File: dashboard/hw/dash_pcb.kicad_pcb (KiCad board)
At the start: 2 copper layers, 180 x 65 mm, 33 parts, among them J1 LCD, J2 DEBUG, J3 LCD_BL, J4 CAR, U1 LPC11C24FBD48, U3 TLV70233_SOT23-5, Y1 12MHz

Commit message: add footprint for TI power chip
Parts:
- added U2: TPS62175, custom_footprints:DQC, F.Cu at (164.5, 78.5)
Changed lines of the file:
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@@
 (kicad_pcb (version 4) (host pcbnew 4.0.7)
   (general
-    (links 88)
-    (no_connects 79)
+    (links 101)
+    (no_connects 89)
     (area 84.924999 54.924999 265.075001 120.075001)
     (thickness 1.6)
@@
     (tracks 83)
     (zones 0)
-    (modules 33)
-    (nets 60)
+    (modules 34)
+    (nets 61)
   )
   (page A4)
@@
   (net 58 +BATT)
   (net 59 "Net-(U1-Pad45)")
+  (net 60 "Net-(L1-Pad1)")
   (net_class Default "This is the default net class."
     (clearance 0.15)
@@
     (add_net "Net-(J2-Pad8)")
     (add_net "Net-(J3-Pad2)")
+    (add_net "Net-(L1-Pad1)")
     (add_net "Net-(R1-Pad1)")
     (add_net "Net-(R10-Pad1)")
@@
     )
   )
+  (module custom_footprints:DQC (layer F.Cu)
+    (at 164.5 78.45)
+    (solder_mask_margin 0.07)
+    (solder_paste_ratio -0.17)
+    (fp_text reference U2 (at 0 2.5) (layer F.SilkS)
+      (effects (font (size 1 1) (thickness 0.15)))
+    )
+    (fp_text value TPS62175 (at 0 -2.5) (layer F.Fab)
+      (effects (font (size 1 1) (thickness 0.15)))
+    )
+    (fp_line (start -1.5 -1.5) (end -1 -1.5) (layer F.SilkS) (width 0.15))
+    (fp_line (start -1.5 -1) (end -1.5 -1.5) (layer F.SilkS) (width 0.15))
+    (fp_line (start -1 1.5) (end 1 1.5) (layer F.CrtYd) (width 0.15))
+    (fp_line (start -1 -1.5) (end 1 -1.5) (layer F.CrtYd) (width 0.15))
+    (pad 1 smd rect (at -0.95 -1) (size 0.5 0.25) (layers F.Cu F.Paste F.Mask)
+      (net 1 GND) (solder_mask_margin 0.07))
+    (pad 2 smd rect (at -0.95 -0.5 180) (size 0.5 0.25) (layers F.Cu F.Paste F.Mask)
+      (net 58 +BATT) (solder_mask_margin 0.07))
+    (pad 3 smd rect (at -0.95 0) (size 0.5 0.25) (layers F.Cu F.Paste F.Mask)
+      (net 58 +BATT) (solder_mask_margin 0.07))
+    (pad 4 smd rect (at -0.95 0.5) (size 0.5 0.25) (layers F.Cu F.Paste F.Mask)
+      (net 1 GND) (solder_mask_margin 0.07))
+    (pad 5 smd rect (at -0.95 1) (size 0.5 0.25) (layers F.Cu F.Paste F.Mask)
+      (net 56 "Net-(R10-Pad1)") (solder_mask_margin 0.07))
+    (pad 6 smd rect (at 0.95 1) (size 0.5 0.25) (layers F.Cu F.Paste F.Mask)
+      (net 1 GND) (solder_mask_margin 0.07))
+    (pad 7 smd rect (at 0.95 0.5) (size 0.5 0.25) (layers F.Cu F.Paste F.Mask)
+      (net 55 /5VPG) (solder_mask_margin 0.07))
+    (pad 8 smd rect (at 0.95 0) (size 0.5 0.25) (layers F.Cu F.Paste F.Mask)
+      (net 2 +5V) (solder_mask_margin 0.07))
+    (pad 9 smd rect (at 0.95 -0.5) (size 0.5 0.25) (layers F.Cu F.Paste F.Mask)
+      (net 60 "Net-(L1-Pad1)") (solder_mask_margin 0.07))
+    (pad 10 smd rect (at 0.95 -1) (size 0.5 0.25) (layers F.Cu F.Paste F.Mask)
+      (net 2 +5V) (solder_mask_margin 0.07))
+    (pad 1 smd rect (at 0 0) (size 0.84 2.4) (layers F.Cu F.Paste F.Mask)
+      (net 1 GND) (solder_paste_margin -0.04) (solder_paste_margin_ratio -0.00001))
+    (pad 1 thru_hole circle (at 0 0) (size 0.4 0.4) (drill 0.2) (layers *.Cu *.Mask)
+      (net 1 GND) (solder_mask_margin 0.04) (solder_paste_margin -0.001) (solder_paste_margin_ratio -0.00001))
+    (pad 1 thru_hole circle (at 0 0.95) (size 0.4 0.4) (drill 0.2) (layers *.Cu *.Mask)
+      (net 1 GND) (solder_mask_margin 0.04) (solder_paste_margin -0.001) (solder_paste_margin_ratio -0.00001))
+    (pad 1 thru_hole circle (at 0 -0.95) (size 0.4 0.4) (drill 0.2) (layers *.Cu *.Mask)
+      (net 1 GND) (solder_mask_margin 0.04) (solder_paste_margin -0.001) (solder_paste_margin_ratio -0.00001))
+  )
   (gr_line (start 265 120) (end 265 55) (layer Edge.Cuts) (width 0.15))

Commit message: add footprint for contrast pot
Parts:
- RV1: footprint Potentiometers:Potentiometer_Trimmer_ACP_CA6h_Vertical -> custom_footprints:Bourns_3362X
- moved RV1 17.3 mm to (252.5, 57.4)
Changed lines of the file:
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@@
-    )
-  )
-  (module Potentiometers:Potentiometer_Trimmer_ACP_CA6h_Vertical (layer F.Cu)
-    (at 244 72.5)
-    (descr "Potentiometer, vertically mounted, Omeg PC16PU, Omeg PC16PU, Omeg PC16PU, Vishay/Spectrol 248GJ/249GJ Single, Vishay/Spectrol 248GJ/249GJ Single, Vishay/Spectrol 248GJ/249GJ Single, Vishay/Spectrol 248GH/249GH Single, Vishay/Spectrol 148/149 Single, Vishay/Spectrol 148/149 Single, Vishay/Spectrol 148/149 Single, Vishay/Spectrol 148A/149A Single with mounting plates, Vishay/Spectrol 148/149 Double, Vishay/Spectrol 148A/149A Double with mounting plates, Piher PC-16 Single, Piher PC-16 Single, Piher PC-16 Single, Piher PC-16SV Single, Piher PC-16 Double, Piher PC-16 Triple, Piher T16H Single, Piher T16L Single, Piher T16H Double, Alps RK163 Single, Alps RK163 Double, Alps RK097 Single, Alps RK097 Double, Bourns PTV09A-2 Single with mounting sleve Single, Bourns PTV09A-1 with mounting sleve Single, Bourns PRS11S Single, Alps RK09K Single with mounting sleve Single, Alps RK09K with mounting sleve Single, Alps RK09L Single, Alps RK09L Single, Alps RK09L Double, Alps RK09L Double, Alps RK09Y Single, Bourns 3339S Single, Bourns 3339S Single, Bourns 3339P Single, Bourns 3339H Single, Vishay T7YA Single, Suntan TSR-3386H Single, Suntan TSR-3386H Single, Suntan TSR-3386P Single, Vishay T73XX Single, Vishay T73XX Single, Vishay T73YP Single, Piher PT-6h Single, Piher PT-6v Single, Piher PT-6v Single, Piher PT-10h2.5 Single, Piher PT-10h5 Single, Piher PT-101h3.8 Single, Piher PT-10v10 Single, Piher PT-10v10 Single, Piher PT-10v5 Single, Piher PT-15h5 Single, Piher PT-15h2.5 Single, Piher PT-15B Single, Piher PT-15hc5 Single, Piher PT-15v12.5 Single, Piher PT-15v12.5 Single, Piher PT-15v15 Single, Piher PT-15v15 Single, ACP CA6h Single, http://www.acptechnologies.com/wp-content/uploads/2016/12/ACP-CAT%C3%81LOGO-ENTERO-2016.pdf")
-    (tags "Potentiometer vertical  Omeg PC16PU  Omeg PC16PU  Omeg PC16PU  Vishay/Spectrol 248GJ/249GJ Single  Vishay/Spectrol 248GJ/249GJ Single  Vishay/Spectrol 248GJ/249GJ Single  Vishay/Spectrol 248GH/249GH Single  Vishay/Spectrol 148/149 Single  Vishay/Spectrol 148/149 Single  Vishay/Spectrol 148/149 Single  Vishay/Spectrol 148A/149A Single with mounting plates  Vishay/Spectrol 148/149 Double  Vishay/Spectrol 148A/149A Double with mounting plates  Piher PC-16 Single  Piher PC-16 Single  Piher PC-16 Single  Piher PC-16SV Single  Piher PC-16 Double  Piher PC-16 Triple  Piher T16H Single  Piher T16L Single  Piher T16H Double  Alps RK163 Single  Alps RK163 Double  Alps RK097 Single  Alps RK097 Double  Bourns PTV09A-2 Single with mounting sleve Single  Bourns PTV09A-1 with mounting sleve Single  Bourns PRS11S Single  Alps RK09K Single with mounting sleve Single  Alps RK09K with mounting sleve Single  Alps RK09L Single  Alps RK09L Single  Alps RK09L Double  Alps RK09L Double  Alps RK09Y Single  Bourns 3339S Single  Bourns 3339S Single  Bourns 3339P Single  Bourns 3339H Single  Vishay T7YA Single  Suntan TSR-3386H Single  Suntan TSR-3386H Single  Suntan TSR-3386P Single  Vishay T73XX Single  Vishay T73XX Single  Vishay T73YP Single  Piher PT-6h Single  Piher PT-6v Single  Piher PT-6v Single  Piher PT-10h2.5 Single  Piher PT-10h5 Single  Piher PT-101h3.8 Single  Piher PT-10v10 Single  Piher PT-10v10 Single  Piher PT-10v5 Single  Piher PT-15h5 Single  Piher PT-15h2.5 Single  Piher PT-15B Single  Piher PT-15hc5 Single  Piher PT-15v12.5 Single  Piher PT-15v12.5 Single  Piher PT-15v15 Single  Piher PT-15v15 Single  ACP CA6h Single")
-    (fp_text reference RV1 (at 0 -2.06) (layer F.SilkS)
-      (effects (font (size 1 1) (thickness 0.15)))
-    )
-    (fp_text value 10k (at 0 7.06) (layer F.Fab)
-      (effects (font (size 1 1) (thickness 0.15)))
-    )
-    (fp_line (start 3.5 -0.65) (end 3.5 5.65) (layer F.Fab) (width 0.1))
-    (fp_line (start 3.5 5.65) (end 0 5.65) (layer F.Fab) (width 0.1))
-    (fp_line (start 0 5.65) (end 0 -0.65) (layer F.Fab) (width 0.1))
-    (fp_line (start 0 -0.65) (end 3.5 -0.65) (layer F.Fab) (width 0.1))
-    (fp_line (start 0 1.5) (end 0 3.5) (layer F.Fab) (width 0.1))
-    (fp_line (start 0 3.5) (end 3.5 3.5) (layer F.Fab) (width 0.1))
-    (fp_line (start 3.5 3.5) (end 3.5 1.5) (layer F.Fab) (width 0.1))
-    (fp_line (start 3.5 1.5) (end 0 1.5) (layer F.Fab) (width 0.1))
-    (fp_line (start 0.873 -0.71) (end 3.56 -0.71) (layer F.SilkS) (width 0.12))
-    (fp_line (start 0.873 5.71) (end 3.56 5.71) (layer F.SilkS) (width 0.12))
-    (fp_line (start 3.56 -0.71) (end 3.56 5.71) (layer F.SilkS) (width 0.12))
-    (fp_line (start -0.061 1.005) (end -0.061 3.996) (layer F.SilkS) (width 0.12))
-    (fp_line (start -0.061 1.44) (end 3.56 1.44) (layer F.SilkS) (width 0.12))
-    (fp_line (start -0.061 3.56) (end 3.56 3.56) (layer F.SilkS) (width 0.12))
-    (fp_line (start -0.061 1.44) (end -0.061 3.56) (layer F.SilkS) (width 0.12))
-    (fp_line (start 3.56 1.44) (end 3.56 3.56) (layer F.SilkS) (width 0.12))
-    (fp_line (start -1.1 -1.1) (end -1.1 6.1) (layer F.CrtYd) (width 0.05))
-    (fp_line (start -1.1 6.1) (end 3.75 6.1) (layer F.CrtYd) (width 0.05))
-    (fp_line (start 3.75 6.1) (end 3.75 -1.1) (layer F.CrtYd) (width 0.05))
-    (fp_line (start 3.75 -1.1) (end -1.1 -1.1) (layer F.CrtYd) (width 0.05))
-    (pad 3 thru_hole circle (at 0 5) (size 1.62 1.62) (drill 0.9) (layers *.Cu *.Mask)
-      (net 1 GND))
-    (pad 2 thru_hole circle (at 2.5 2.5) (size 1.62 1.62) (drill 0.9) (layers *.Cu *.Mask)
-      (net 3 /LCD_V0))
-    (pad 1 thru_hole circle (at 0 0) (size 1.62 1.62) (drill 0.9) (layers *.Cu *.Mask)
-      (net 15 /LCD_VEE))
-    (model Potentiometers.3dshapes/Potentiometer_Trimmer_ACP_CA6h_Vertical.wrl
-      (at (xyz 0 0 0))
-      (scale (xyz 0.393701 0.393701 0.393701))
-      (rotate (xyz 0 0 0))
     )
   )
@@
       (net 1 GND) (solder_mask_margin 0.04) (solder_paste_margin -0.001) (solder_paste_margin_ratio -0.00001))
   )
+  (module custom_footprints:Bourns_3362X (layer F.Cu)
+    (at 252.476 57.404)
+    (fp_text reference RV1 (at -1.27 3.302) (layer F.SilkS)
+      (effects (font (size 1 1) (thickness 0.15)))
+    )
+    (fp_text value 10k (at 0 -3.048) (layer F.Fab)
+      (effects (font (size 1 1) (thickness 0.15)))
+    )
+    (fp_line (start -3.302 -2.286) (end -3.302 1.016) (layer F.SilkS) (width 0.15))
+    (fp_line (start 3.302 -2.286) (end -3.302 -2.286) (layer F.SilkS) (width 0.15))
+    (fp_line (start 3.302 2.286) (end 3.302 -2.286) (layer F.SilkS) (width 0.15))
+    (fp_line (start 1.778 2.286) (end 3.302 2.286) (layer F.SilkS) (width 0.15))
+    (fp_line (start 1.778 1.778) (end 1.778 2.286) (layer F.SilkS) (width 0.15))
+    (fp_line (start -1.778 1.778) (end 1.778 1.778) (layer F.SilkS) (width 0.15))
+    (fp_line (start -1.778 2.286) (end -1.778 1.778) (layer F.SilkS) (width 0.15))
+    (fp_line (start -3.302 2.286) (end -1.778 2.286) (layer F.SilkS) (width 0.15))
+    (fp_line (start -3.302 1.016) (end -3.302 2.286) (layer F.SilkS) (width 0.15))
+    (fp_line (start 3.302 2.286) (end 0 2.286) (layer F.CrtYd) (width 0.15))
+    (fp_line (start 3.302 -2.286) (end 3.302 2.286) (layer F.CrtYd) (width 0.15))
+    (fp_line (start -3.302 -2.286) (end 3.302 -2.286) (layer F.CrtYd) (width 0.15))
+    (fp_line (start -3.302 2.286) (end -3.302 -2.286) (layer F.CrtYd) (width 0.15))
+    (fp_line (start 0 2.286) (end -3.302 2.286) (layer F.CrtYd) (width 0.15))
+    (pad 2 thru_hole circle (at 0 -1.27) (size 1 1) (drill 0.5) (layers *.Cu *.Mask)
+      (net 3 /LCD_V0))
+    (pad 3 thru_hole circle (at -2.54 1.27) (size 1 1) (drill 0.5) (layers *.Cu *.Mask)
+      (net 1 GND))
+    (pad 1 thru_hole circle (at 2.54 1.27) (size 1 1) (drill 0.5) (layers *.Cu *.Mask)
+      (net 15 /LCD_VEE))
+  )
   (gr_line (start 265 120) (end 265 55) (layer Edge.Cuts) (width 0.15))

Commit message: add footprint for inductor
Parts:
- added L1: 10u, custom_footprints:Coilcraft_LPS4018, F.Cu at (170.7, 71.6)
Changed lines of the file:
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@@
 (kicad_pcb (version 4) (host pcbnew 4.0.7)
   (general
-    (links 101)
-    (no_connects 89)
+    (links 109)
+    (no_connects 97)
     (area 84.924999 54.924999 265.075001 120.075001)
     (thickness 1.6)
@@
     (tracks 83)
     (zones 0)
-    (modules 34)
+    (modules 35)
     (nets 61)
   )
@@
       (net 15 /LCD_VEE))
   )
+  (module custom_footprints:Coilcraft_LPS4018 (layer F.Cu)
+    (at 170.688 71.628)
+    (fp_text reference L1 (at 0 3.1) (layer F.SilkS)
+      (effects (font (size 1 1) (thickness 0.15)))
+    )
+    (fp_text value 10u (at 0 -3) (layer F.Fab)
+      (effects (font (size 1 1) (thickness 0.15)))
+    )
+    (pad 2 smd trapezoid (at 1.89 0) (size 0.56 3.34) (rect_delta 0.55 0 ) (layers F.Cu F.Paste F.Mask)
+      (net 2 +5V))
+    (pad 2 smd rect (at 1.17 -1.45 180) (size 0.89 1) (layers F.Cu F.Paste F.Mask)
+      (net 2 +5V))
+    (pad 2 smd rect (at 1.17 1.44 180) (size 0.89 1) (layers F.Cu F.Paste F.Mask)
+      (net 2 +5V))
+    (pad 1 smd rect (at -1.17 1.44) (size 0.89 1) (layers F.Cu F.Paste F.Mask)
+      (net 60 "Net-(L1-Pad1)"))
+    (pad 1 smd trapezoid (at -1.89 0 180) (size 0.56 3.34) (rect_delta 0.55 0 ) (layers F.Cu F.Paste F.Mask)
+      (net 60 "Net-(L1-Pad1)"))
+    (pad 1 smd rect (at -1.17 -1.44) (size 0.89 1) (layers F.Cu F.Paste F.Mask)
+      (net 60 "Net-(L1-Pad1)"))
+    (pad 2 smd rect (at 1.45 -0.02) (size 0.33 2) (layers F.Cu F.Paste F.Mask)
+      (net 2 +5V))
+    (pad 1 smd rect (at -1.45 0) (size 0.33 2) (layers F.Cu F.Paste F.Mask)
+      (net 60 "Net-(L1-Pad1)"))
+  )
   (gr_line (start 265 120) (end 265 55) (layer Edge.Cuts) (width 0.15))

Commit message: reset automatically when power isn't good
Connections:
- R7 pad 1: /MCU_~RESET -> /5VPG
- U1 pad 3: /MCU_~RESET -> /5VPG

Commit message: lay out power bits
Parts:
- moved R7 66.1 mm to (224.3, 108.4), turned to 180 degrees
- moved J2 66.1 mm to (214.5, 102.0)
- moved R1 66.1 mm to (220.0, 103.8)
- moved R3 66.1 mm to (219.8, 99.0)
- moved R5 66.1 mm to (224.2, 101.0)
- moved R6 66.1 mm to (223.8, 105.0)
- moved J3 38.5 mm to (157.0, 106.5), turned to 180 degrees
- moved J4 22.8 mm to (157.0, 86.6)
- moved R11 20.1 mm to (168.0, 103.0), turned to 180 degrees
- moved R12 20.1 mm to (168.0, 108.0), turned to 180 degrees
- moved C9 17.8 mm to (171.0, 84.2), turned to 180 degrees
- moved C8 16.8 mm to (168.2, 86.8), turned to 90 degrees
- moved R8 14.3 mm to (174.2, 90.0), turned to 180 degrees
- moved L1 14.3 mm to (175.1, 85.2), turned to 90 degrees
- moved U2 11.6 mm to (171.0, 88.0)
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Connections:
- U3 pad 4: Net-(U3-Pad4) -> +3V3
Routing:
- net +5V: track 0.00 -> 31.1 mm, vias 0 -> 2
- net +BATT: track 0.00 -> 13.9 mm
- net GND: track 0.00 -> 11.5 mm, vias 0 -> 5
- net /5VPG: track 0.00 -> 10.9 mm, vias 0 -> 2
- net Net-(L1-Pad1): track 0.00 -> 7.24 mm
- net +3V3: track 0.00 -> 5.73 mm
- net Net-(R10-Pad1): track 0.00 -> 4.02 mm
- added copper zone on F.Cu, net +5V
- added copper zone on B.Cu, net GND
- added copper zone on F.Cu, net GND
- added copper zone on F.Cu, net Net-(L1-Pad1)

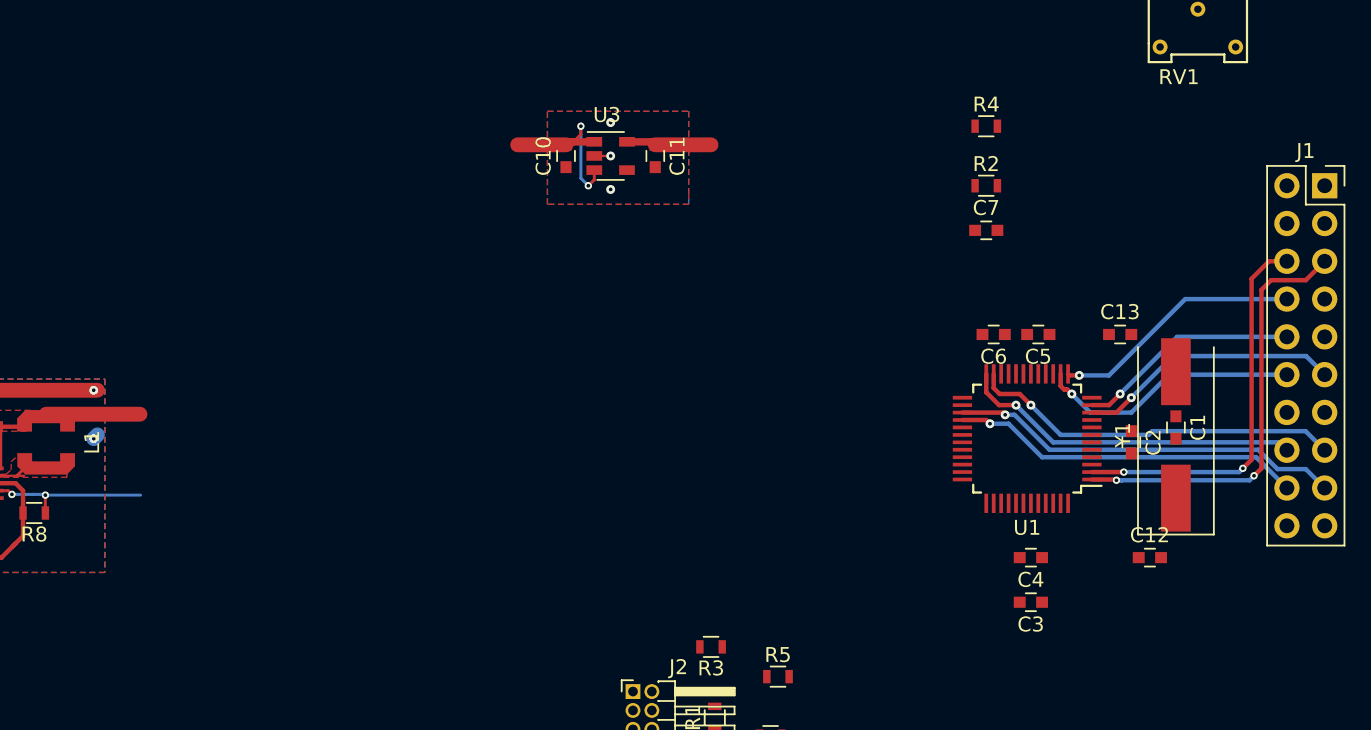
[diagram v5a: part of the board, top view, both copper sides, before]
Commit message: lay out passives and xtal around the micro
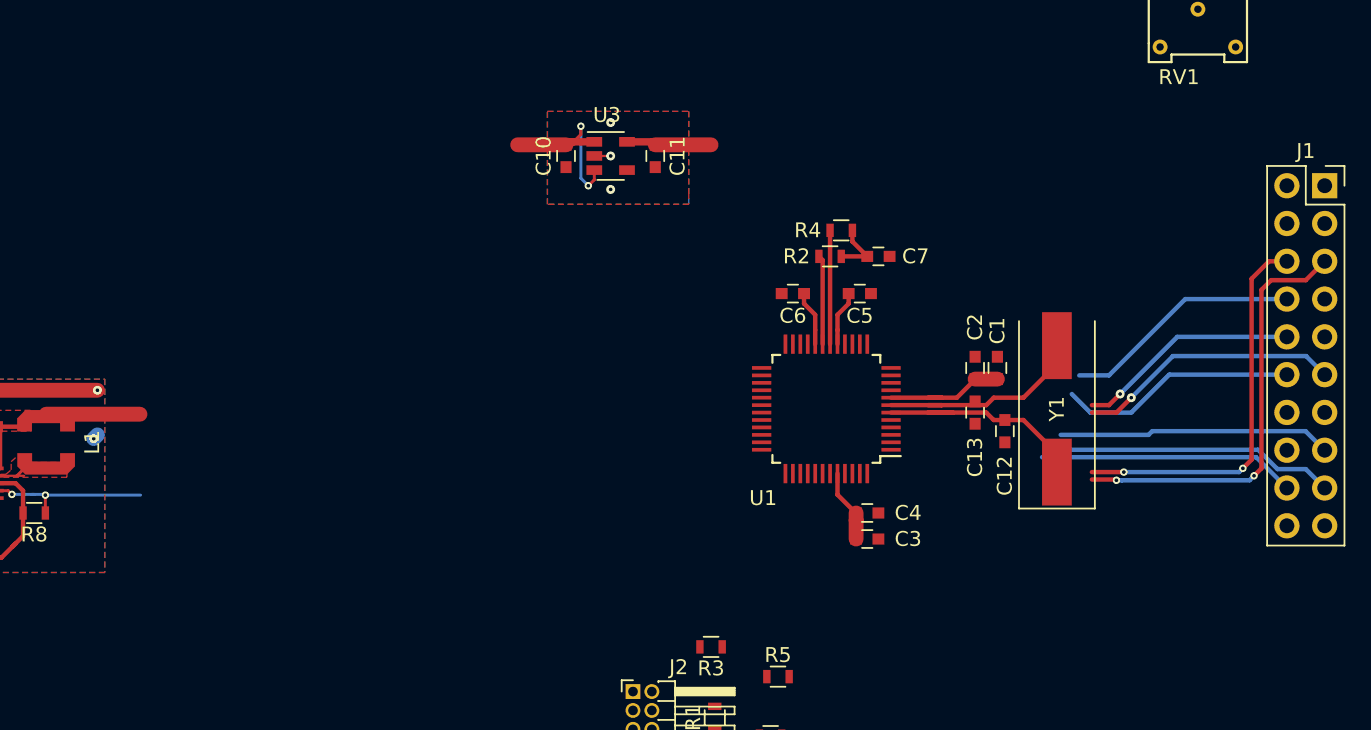
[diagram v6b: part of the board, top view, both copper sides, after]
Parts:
- moved C6 13.8 mm to (225.2, 75.2)
- moved U1 13.6 mm to (227.5, 83.0)
- moved C12 12.9 mm to (239.5, 84.5), turned to 90 degrees
- moved C1 12.6 mm to (239.0, 80.2), turned to 90 degrees
- moved C5 12.3 mm to (229.8, 75.2), turned to 0 degrees
- moved R4 12.0 mm to (228.5, 71.0), turned to 180 degrees
- moved C3 11.8 mm to (230.2, 91.8), turned to 0 degrees
- moved C2 11.6 mm to (237.5, 80.2), turned to 90 degrees
- moved R2 11.5 mm to (227.8, 72.8), turned to 180 degrees
- moved C4 11.4 mm to (230.2, 90.0), turned to 0 degrees
- moved C13 11.1 mm to (237.5, 83.2), turned to 90 degrees
- moved Y1 8.19 mm to (243.0, 83.0)
- moved C7 7.46 mm to (231.0, 72.8)
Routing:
- net /LCD_DB5: track 23.1 -> 0.75 mm, vias 1 -> 0
- net +3V3: track 5.73 -> 23.5 mm
- net /XTALIN: track 0.00 -> 14.9 mm
- net /XTALOUT: track 0.00 -> 14.4 mm
- net /CANL: track 0.00 -> 7.65 mm
- net /LCD_DB6: track 26.5 -> 19.6 mm, vias 1 -> 0
- net /LCD_DB4: track 25.1 -> 18.4 mm, vias 1 -> 0
- net /LCD_DB7: track 23.7 -> 17.3 mm, vias 1 -> 0
- net /CANH: track 0.00 -> 6.00 mm
- net Net-(C7-Pad1): track 0.00 -> 3.91 mm
- net +5V: track 31.1 -> 34.9 mm
- net /LCD_DB1: track 17.8 -> 16.0 mm, vias 1 -> 0
- net /LCD_~RST: track 13.9 -> 15.0 mm
- net /LCD_DB2: track 1.15 -> 0.00 mm
- net /LCD_C/~D: track 16.9 -> 16.1 mm, vias 1 -> 0
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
